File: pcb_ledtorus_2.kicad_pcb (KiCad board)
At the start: 4 copper layers, 149 x 149 mm, 280 parts, among them P1 CONN_02X04, P2 CONN_6, P3 MICRO-SD, P4 CONN_2, P5 KNUSB, P6 CONN_12, P7 CONN_01X03, U1 STM32F46X_LQFP176, U10 TLC5955, U11 TLC5955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

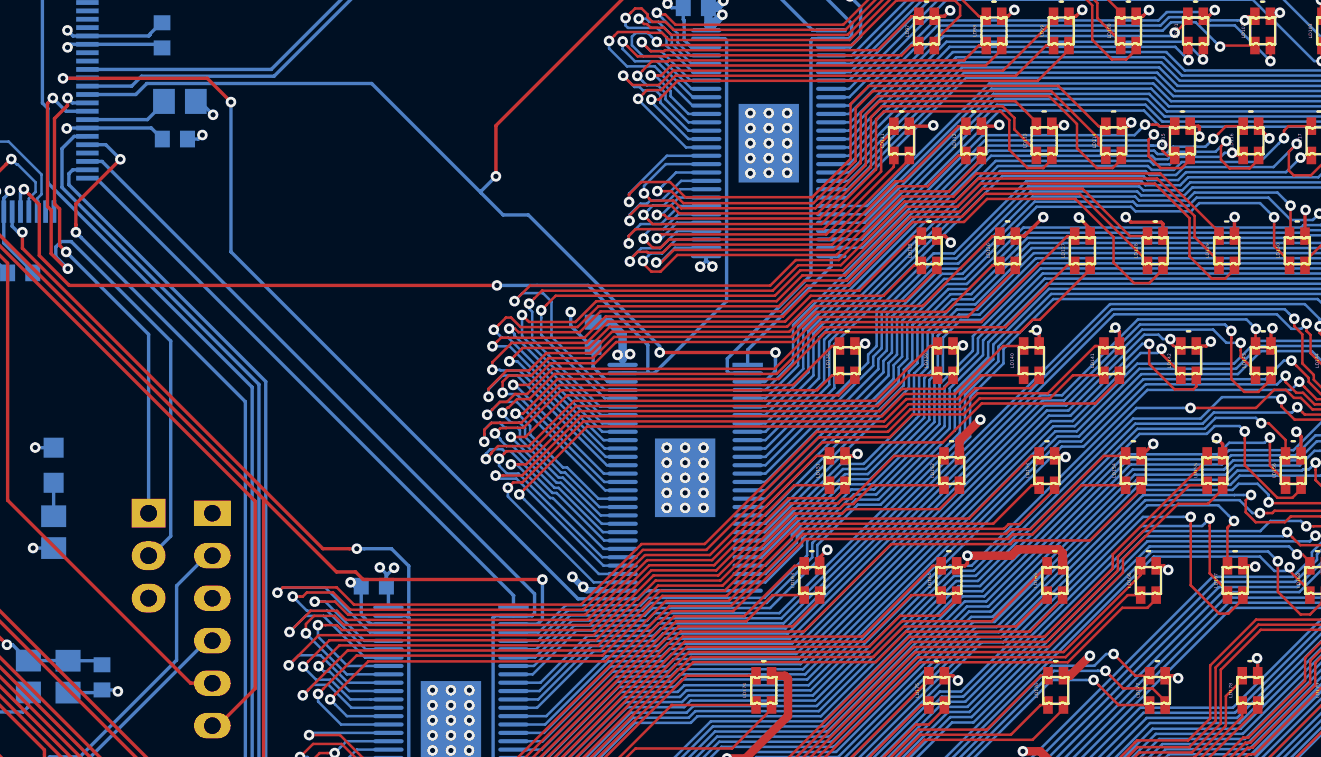
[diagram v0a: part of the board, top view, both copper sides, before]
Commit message: Cleanup back routing on U11
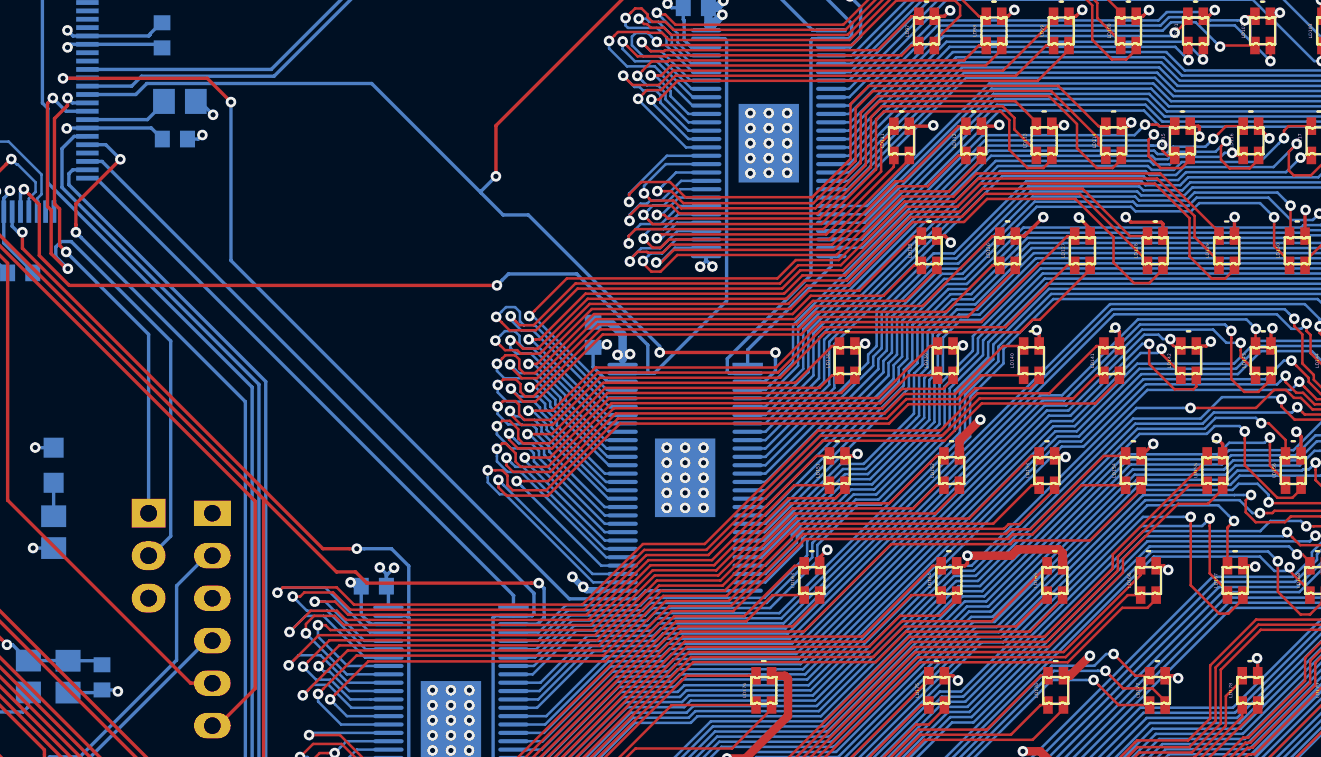
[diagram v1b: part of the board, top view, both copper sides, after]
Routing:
- net /LEDs/led138b: track 35.8 -> 28.7 mm
- net /LEDs/led126b: track 45.8 -> 39.5 mm
- net /LEDs/led129r: track 56.6 -> 62.6 mm
- net /LEDs/led127b: track 50.1 -> 44.8 mm
- net /LEDs/led139b: track 40.7 -> 35.4 mm
- net /LEDs/led125b: track 38.5 -> 34.4 mm
- net /LEDs/led140g: track 43.1 -> 47.0 mm
- net /LEDs/led140r: track 42.3 -> 45.9 mm
- net /LEDs/led129b: track 57.3 -> 53.9 mm
- net /LEDs/led128r: track 55.2 -> 58.0 mm
- net /LEDs/led140b: track 44.6 -> 42.1 mm
- net /LEDs/led127g: track 47.7 -> 49.8 mm
- net /LEDs/led139g: track 38.4 -> 40.3 mm
- net /LEDs/led128b: track 51.3 -> 49.4 mm
- net /LEDs/led126g: track 42.6 -> 44.5 mm
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
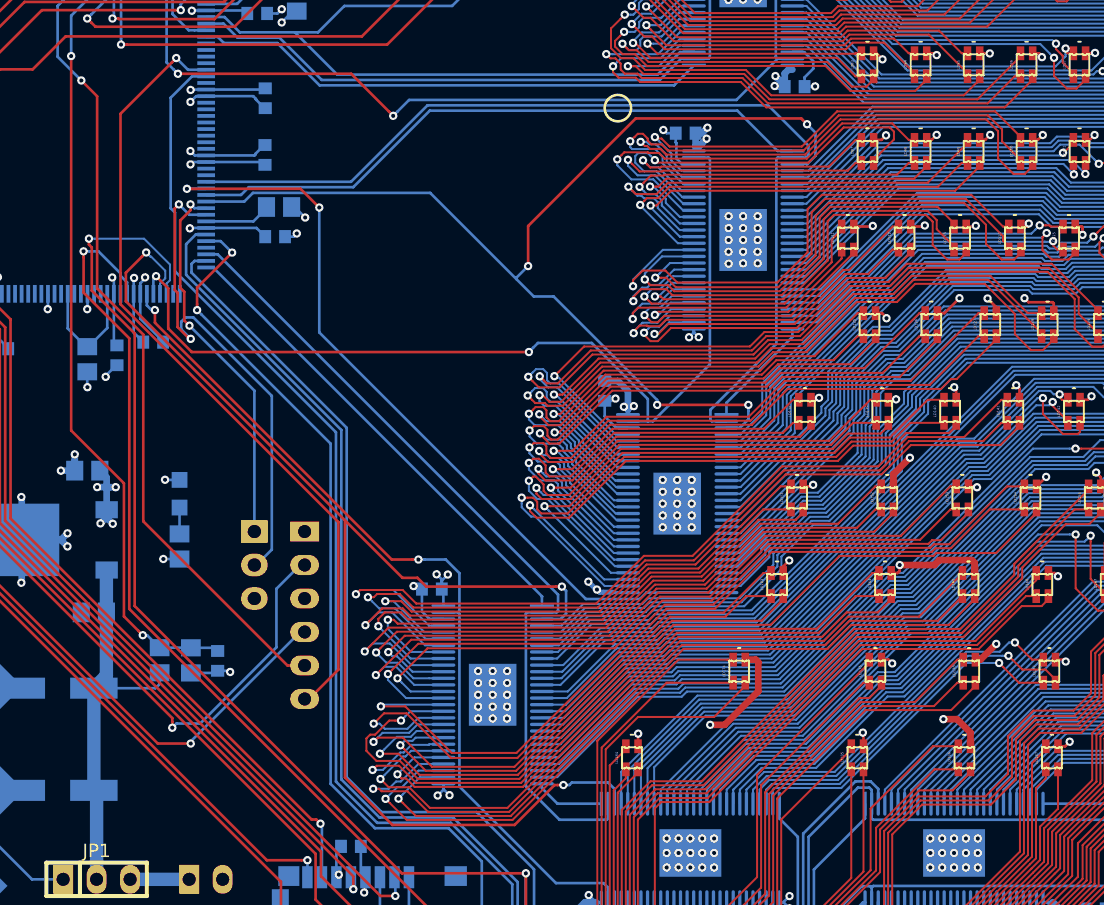
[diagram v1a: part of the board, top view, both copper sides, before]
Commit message: Cleanup back routing on U12
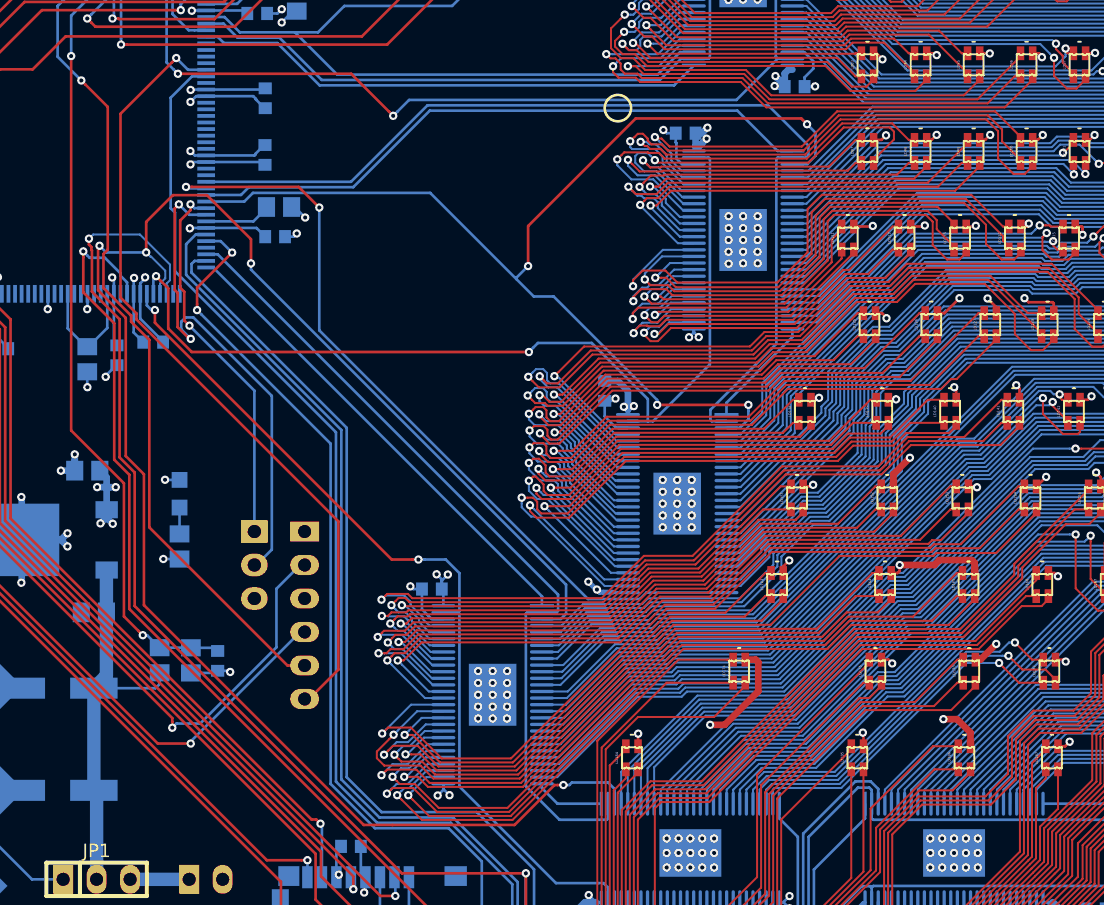
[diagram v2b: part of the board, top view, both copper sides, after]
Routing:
- net /lat5: track 98.6 -> 134.5 mm, vias 3 -> 4
- net /LEDs/led154g: track 64.7 -> 59.3 mm
- net /LEDs/led141b: track 64.2 -> 60.0 mm
- net /LEDs/led141g: track 61.9 -> 57.8 mm
- net /LEDs/led151b: track 44.4 -> 40.8 mm
- net /LEDs/led141r: track 59.9 -> 56.9 mm
- net /LEDs/led151g: track 41.7 -> 39.1 mm
- net /LEDs/led151r: track 41.0 -> 38.4 mm
- net /LEDs/led152b: track 51.2 -> 48.9 mm
- net /LEDs/led163r: track 42.5 -> 40.3 mm
- net /LEDs/led154r: track 68.0 -> 66.1 mm
- net /LEDs/led164r: track 52.1 -> 50.3 mm
- net /LEDs/led152g: track 48.7 -> 46.9 mm
- net /LEDs/led165r: track 57.8 -> 56.0 mm
- net /LEDs/led165b: track 59.0 -> 57.3 mm
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
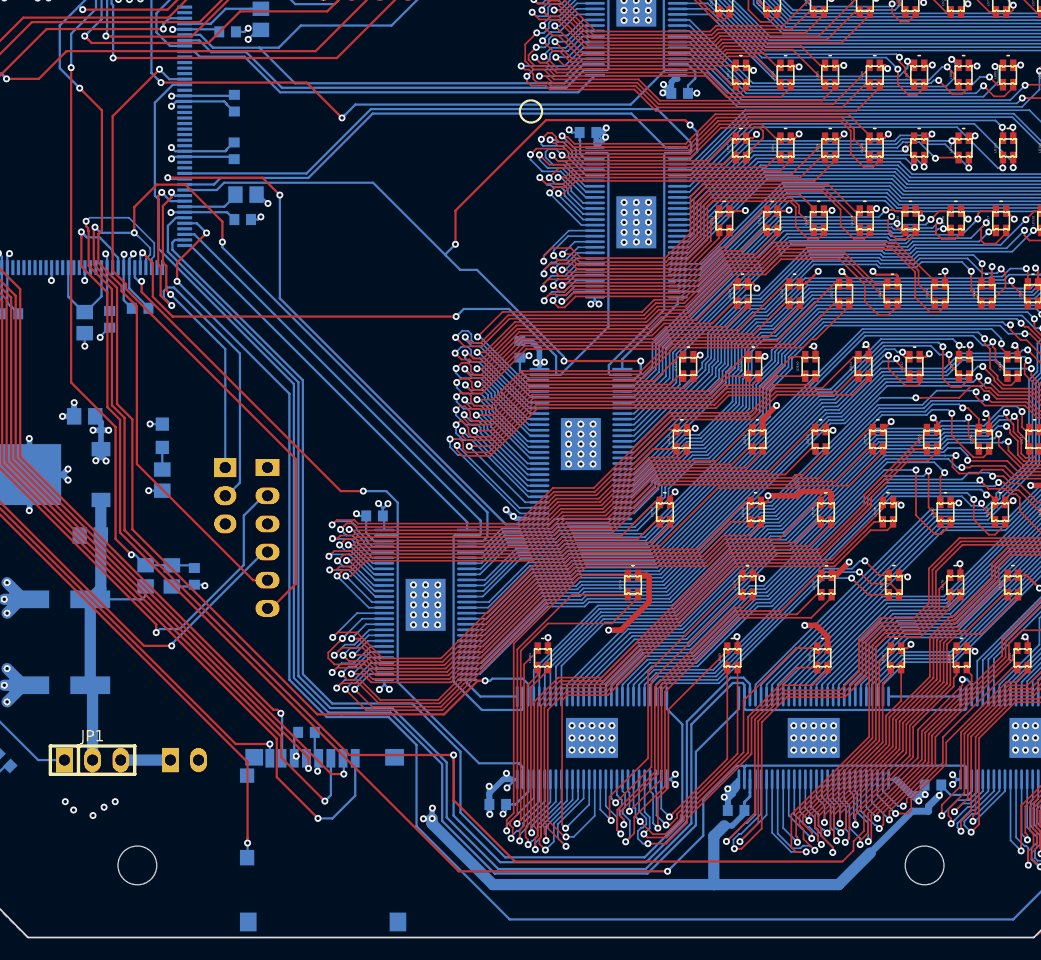
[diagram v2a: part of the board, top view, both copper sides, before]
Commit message: Cleanup back routing on U13
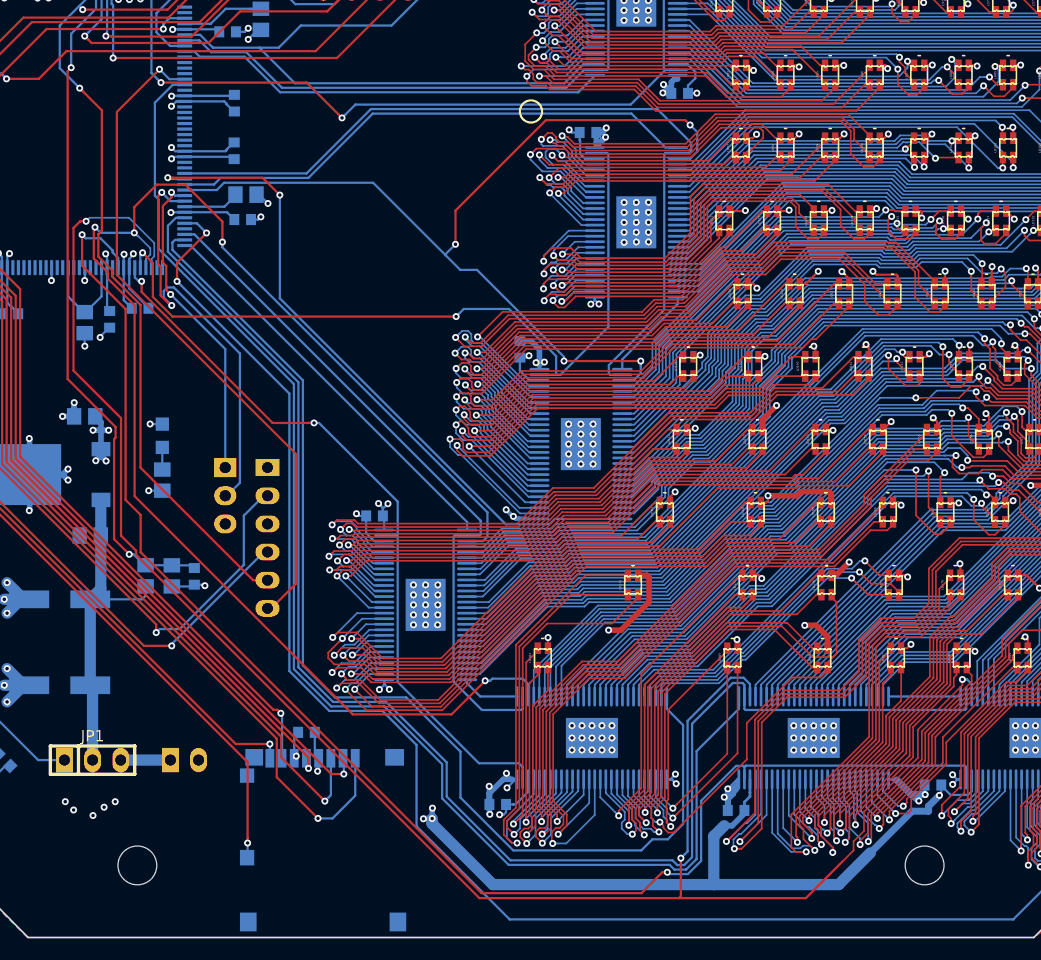
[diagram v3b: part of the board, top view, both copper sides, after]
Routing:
- net /lat6: track 188.8 -> 168.6 mm
- net /LEDs/led155b: track 67.3 -> 61.5 mm
- net /LEDs/led166b: track 59.1 -> 53.4 mm
- net /LEDs/led176r: track 40.0 -> 45.0 mm
- net /LEDs/led175g: track 26.0 -> 30.2 mm
- net /LEDs/led184b: track 24.8 -> 20.9 mm
- net /LEDs/led174b: track 35.6 -> 39.2 mm
- net /LEDs/led186r: track 32.2 -> 28.7 mm
- net /LEDs/led176g: track 33.1 -> 36.0 mm
- net /LEDs/led186g: track 29.5 -> 32.1 mm
- net /gsclk6: track 131.1 -> 133.5 mm
- net /LEDs/led176b: track 37.3 -> 39.7 mm
- net /LEDs/led186b: track 30.4 -> 32.7 mm
- net /LEDs/led166r: track 53.6 -> 55.7 mm
- net /LEDs/led166g: track 56.1 -> 58.2 mm
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
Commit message: Cleanup back routing on U14
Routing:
- net /LEDs/led178r: track 40.5 -> 33.6 mm
- net /LEDs/led178b: track 42.4 -> 37.3 mm
- net /LEDs/led178g: track 36.1 -> 31.5 mm
- net /LEDs/led187r: track 26.4 -> 22.5 mm
- net /LEDs/led171b: track 57.3 -> 53.5 mm
- net /LEDs/led180b: track 37.4 -> 35.1 mm
- net /LEDs/led188r: track 26.8 -> 24.6 mm
- net /LEDs/led189r: track 23.0 -> 21.6 mm
- net /LEDs/led189b: track 24.6 -> 23.2 mm
- net /LEDs/led180r: track 34.5 -> 33.1 mm
- net /LEDs/led179b: track 36.8 -> 35.6 mm
- net /LEDs/led188b: track 27.9 -> 26.7 mm
- net /LEDs/led170r: track 62.9 -> 61.8 mm
- net /LEDs/led180g: track 31.6 -> 30.5 mm
- net /LEDs/led170g: track 60.0 -> 58.9 mm
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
